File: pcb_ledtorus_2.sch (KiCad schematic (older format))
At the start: 15 parts, among them P1 CONN_02X04, P2 CONN_6, P3 MICRO-SD, P6 CONN_12, U4 STM32F46X_LQFP176, U5 US4881_HALL

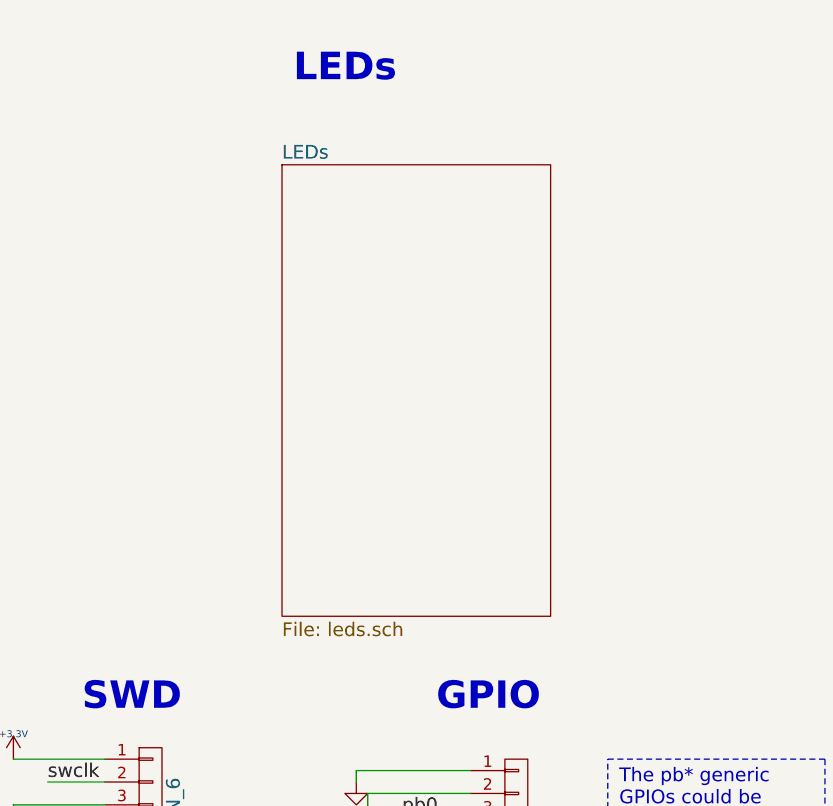
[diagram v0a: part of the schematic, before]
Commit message: Fix sin/sclk/sout/lat/gsclk 1-6 pins and labels.
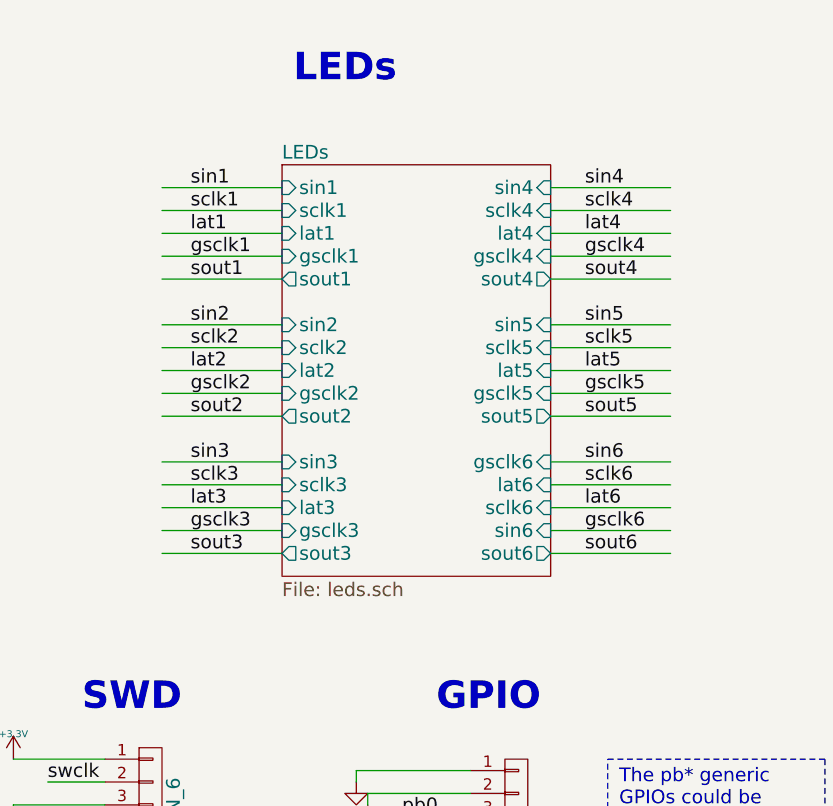
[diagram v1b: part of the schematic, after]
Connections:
- net labels added: lat4, lat5, lat6
- wire segments 128 -> 158
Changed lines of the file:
@@
 	5600 1600 5250 1600
 $Sheet
-S 8675 1675 1175 1975
+S 8675 1675 1175 1800
 U 5636686F
 F0 "LEDs" 60
 F1 "leds.sch" 60
+F2 "gsclk1" I L 8675 2075 60
+F3 "lat1" I L 8675 1975 60
+F4 "sclk1" I L 8675 1875 60
+F5 "sin1" I L 8675 1775 60
+F6 "sout1" O L 8675 2175 60
+F7 "gsclk2" I L 8675 2675 60
+F8 "lat2" I L 8675 2575 60
+F9 "sclk2" I L 8675 2475 60
+F10 "sin2" I L 8675 2375 60
+F11 "sout2" O L 8675 2775 60
+F12 "gsclk3" I L 8675 3275 60
+F13 "lat3" I L 8675 3175 60
+F14 "sclk3" I L 8675 3075 60
+F15 "sin3" I L 8675 2975 60
+F16 "sout3" O L 8675 3375 60
+F17 "gsclk4" I R 9850 2075 60
+F18 "lat4" I R 9850 1975 60
+F19 "sclk4" I R 9850 1875 60
+F20 "sin4" I R 9850 1775 60
+F21 "sout4" O R 9850 2175 60
+F22 "gsclk5" I R 9850 2675 60
+F23 "lat5" I R 9850 2575 60
+F24 "sclk5" I R 9850 2475 60
+F25 "sin5" I R 9850 2375 60
+F26 "sout5" O R 9850 2775 60
+F27 "gsclk6" I R 9850 2975 60
+F28 "lat6" I R 9850 3075 60
+F29 "sclk6" I R 9850 3175 60
+F30 "sin6" I R 9850 3275 60
+F31 "sout6" O R 9850 3375 60
 $EndSheet
+Wire Wire Line
+	8675 1775 8150 1775
+Wire Wire Line
+	8675 1875 8150 1875
+Wire Wire Line
+	8675 1975 8150 1975
+Wire Wire Line
+	8675 2075 8150 2075
+Wire Wire Line
+	8675 2175 8150 2175
+Wire Wire Line
+	8675 2375 8150 2375
+Wire Wire Line
+	8675 2475 8150 2475
+Wire Wire Line
+	8675 2575 8150 2575
+Wire Wire Line
+	8675 2675 8150 2675
+Wire Wire Line
+	8675 2775 8150 2775
+Wire Wire Line
+	8675 2975 8150 2975
+Wire Wire Line
+	8675 3075 8150 3075
+Wire Wire Line
+	8675 3175 8150 3175
+Wire Wire Line
+	8675 3275 8150 3275
+Wire Wire Line
+	8675 3375 8150 3375
+Wire Wire Line
+	10375 1775 9850 1775
+Wire Wire Line
+	10375 1875 9850 1875
+Wire Wire Line
+	10375 1975 9850 1975
+Wire Wire Line
+	10375 2075 9850 2075
+Wire Wire Line
+	10375 2175 9850 2175
+Wire Wire Line
+	10375 2375 9850 2375
+Wire Wire Line
+	10375 2475 9850 2475
+Wire Wire Line
+	10375 2575 9850 2575
+Wire Wire Line
+	10375 2675 9850 2675
+Wire Wire Line
+	10375 2775 9850 2775
+Wire Wire Line
+	10375 2975 9850 2975
+Wire Wire Line
+	10375 3075 9850 3075
+Wire Wire Line
+	10375 3175 9850 3175
+Wire Wire Line
+	10375 3275 9850 3275
+Wire Wire Line
+	10375 3375 9850 3375
+Text Label 8275 1775 0    60   ~ 0
+sin1
+Text Label 8275 2375 0    60   ~ 0
+sin2
+Text Label 8275 2975 0    60   ~ 0
+sin3
+Text Label 8275 1875 0    60   ~ 0
+sclk1
+Text Label 8275 2475 0    60   ~ 0
+sclk2
+Text Label 8275 3075 0    60   ~ 0
+sclk3
+Text Label 8275 1975 0    60   ~ 0
+lat1
+Text Label 8275 2575 0    60   ~ 0
+lat2
+Text Label 8275 3175 0    60   ~ 0
+lat3
+Text Label 8275 2075 0    60   ~ 0
+gsclk1
+Text Label 8275 2675 0    60   ~ 0
+gsclk2
+Text Label 8275 3275 0    60   ~ 0
+gsclk3
+Text Label 8275 2175 0    60   ~ 0
+sout1
+Text Label 8275 2775 0    60   ~ 0
+sout2
+Text Label 8275 3375 0    60   ~ 0
+sout3
+Text Label 10000 1775 0    60   ~ 0
+sin4
+Text Label 10000 2375 0    60   ~ 0
+sin5
+Text Label 10000 2975 0    60   ~ 0
+sin6
+Text Label 10000 1875 0    60   ~ 0
+sclk4
+Text Label 10000 2475 0    60   ~ 0
+sclk5
+Text Label 10000 3075 0    60   ~ 0
+sclk6
+Text Label 10000 1975 0    60   ~ 0
+lat4
+Text Label 10000 2575 0    60   ~ 0
+lat5
+Text Label 10000 3175 0    60   ~ 0
+lat6
+Text Label 10000 2075 0    60   ~ 0
+gsclk4
+Text Label 10000 2675 0    60   ~ 0
+gsclk5
+Text Label 10000 3275 0    60   ~ 0
+gsclk6
+Text Label 10000 2175 0    60   ~ 0
+sout4
+Text Label 10000 2775 0    60   ~ 0
+sout5
+Text Label 10000 3375 0    60   ~ 0
+sout6
 $EndSCHEMATC

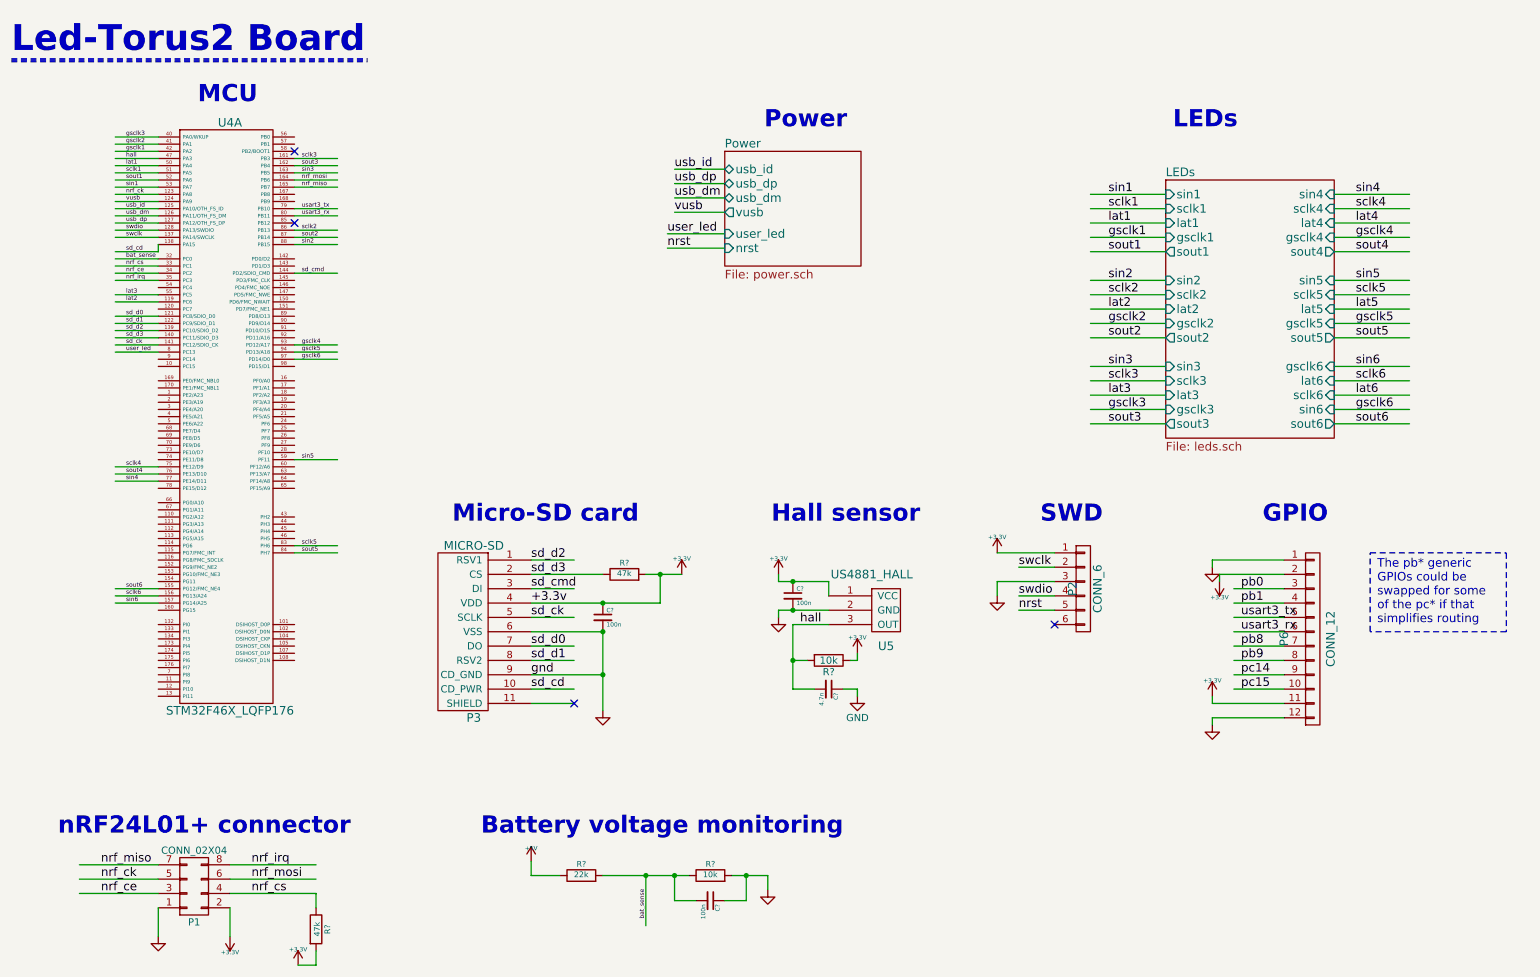
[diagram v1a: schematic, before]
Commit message: Fix alignment of everything to 50 mil
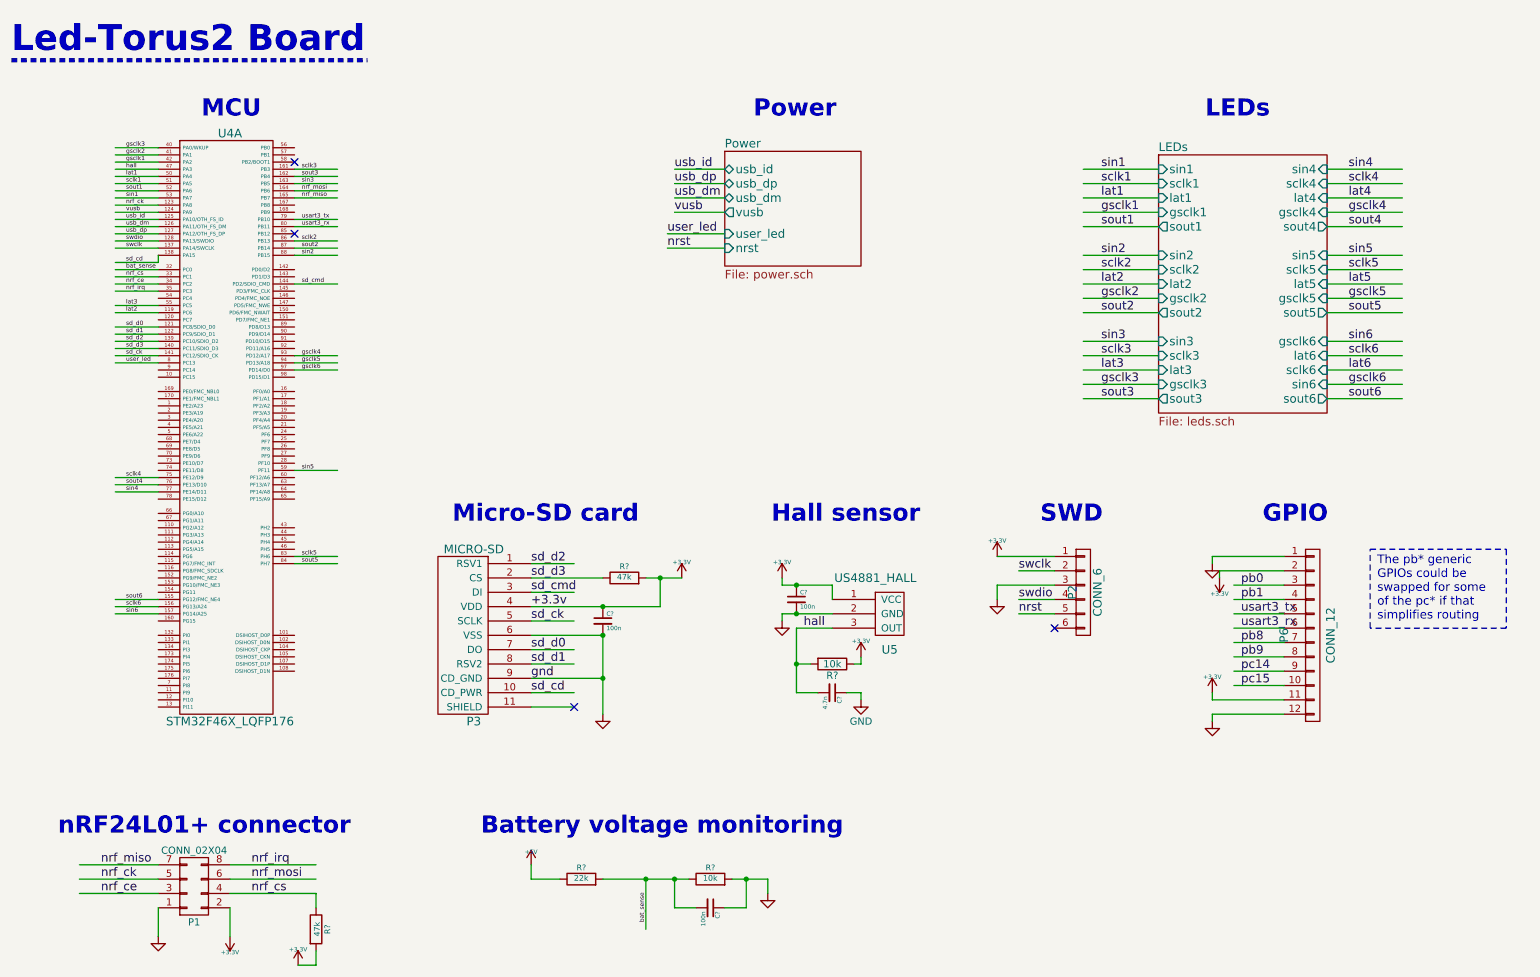
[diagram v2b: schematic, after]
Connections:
- wire segments 158 -> 167
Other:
- moved on the sheet: C?, P2, P3, P6, R?, U4A, U5

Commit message: Misc. small fixes, DRC (almost) passes now.
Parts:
- gave numbers to parts that had none: 9
- renumbered U4 to U1, U5 to U2
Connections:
- net labels removed: pb0, pb1, pb8, pb9, pc14, pc15
- wire segments 167 -> 155
- no-connect marks 4 -> 89

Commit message: Couple small fixes and tweaks.
Some resistors added on inputs connected directly to power lines.
Few labels added.
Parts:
- added R8: 10k, symbol R_Small
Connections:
- net labels added: usb_5v
- wire segments 155 -> 156
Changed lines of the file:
@@
 user_led
 Text Label 5250 1900 0    60   ~ 0
-vusb
+usb_5v
 Text Label 5200 2150 0    60   ~ 0
 nrst
@@
 Text Label 2650 4250 0    30   ~ 0
 lat6
+$Comp
+L R_Small R8
+U 1 1 5638A770
+P 1250 1900
+F 0 "R8" H 1280 1920 30  0000 L CNN
+F 1 "10k" V 1250 1850 30  0000 L CNN
+F 2 "" H 1250 1900 60  0000 C CNN
+F 3 "" H 1250 1900 60  0000 C CNN
+	1    1250 1900
+	0    1    1    0
+$EndComp
+Wire Wire Line
+	1150 1900 975  1900
+Text Label 1000 1900 0    30   ~ 0
+usb_5v
 $EndSCHEMATC

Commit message: Basic netlist with footprint assignment and import into pcbnew
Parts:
- P1: footprint (none) -> w_pin_strip:pin_socket_4x2
- R8: footprint (none) -> w_smd_resistors:r_0805
- U1: footprint (none) -> w_smd_lqfp:LQFP-176
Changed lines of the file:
@@
 F 0 "U1" H 2150 5450 60  0000 C CNN
 F 1 "STM32F46X_LQFP176" H 2150 1350 60  0000 C CNN
-F 2 "" H 2150 3700 60  0000 C CNN
+F 2 "w_smd_lqfp:LQFP-176" H 2150 3700 60  0001 C CNN
 F 3 "" H 2150 3700 60  0000 C CNN
 	1    2150 3400
@@
 F 0 "P1" H 1900 6850 50  0000 C CNN
 F 1 "CONN_02X04" H 1900 6350 50  0000 C CNN
-F 2 "" H 1900 5400 60  0000 C CNN
+F 2 "w_pin_strip:pin_socket_4x2" H 1900 5400 60  0001 C CNN
 F 3 "" H 1900 5400 60  0000 C CNN
 	1    1900 6600
@@
 F 0 "R8" H 1280 1920 30  0000 L CNN
 F 1 "10k" V 1250 1850 30  0000 L CNN
-F 2 "" H 1250 1900 60  0000 C CNN
+F 2 "w_smd_resistors:r_0805" H 1250 1900 60  0001 C CNN
 F 3 "" H 1250 1900 60  0000 C CNN
 	1    1250 1900

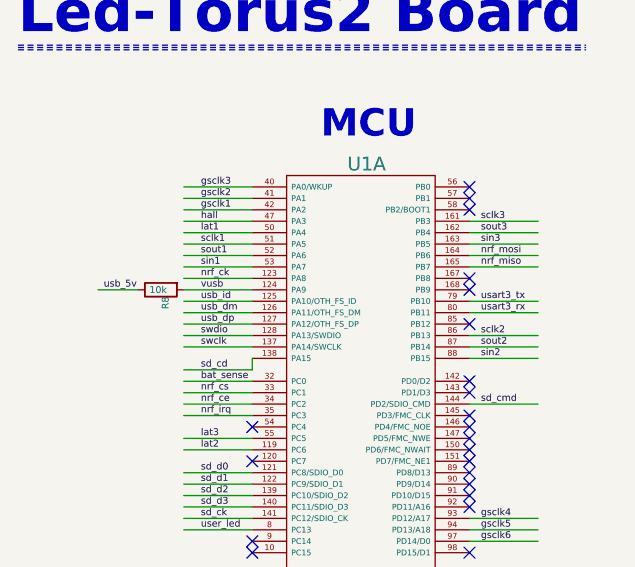
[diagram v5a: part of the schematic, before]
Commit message: Small component changes.
Fix couple of missing footprints. Make 100nF caps 0603.

Some very rough component placement to avoid overlap.
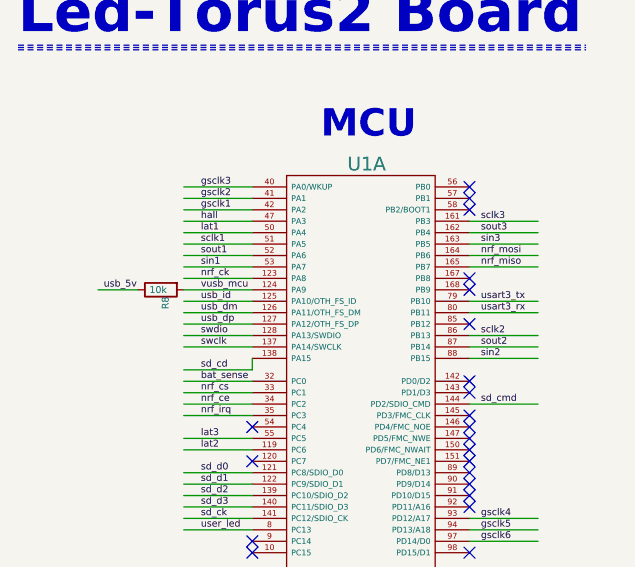
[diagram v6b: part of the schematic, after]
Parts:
- C1, C2, C4: footprint w_smd_cap:c_0805 -> w_smd_cap:c_0603
- U2: footprint Discret:TO92 -> TO_SOT_Packages_THT:TO-92_Inline_Narrow_Oval
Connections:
- net labels added: vusb_mcu
- net labels removed: vusb
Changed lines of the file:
@@
 F 0 "C2" H 4775 4800 30  0000 L CNN
 F 1 "100n" H 4775 4700 30  0000 L CNN
-F 2 "w_smd_cap:c_0805" H 4750 4750 60  0001 C CNN
+F 2 "w_smd_cap:c_0603" H 4750 4750 60  0001 C CNN
 F 3 "" H 4750 4750 60  0000 C CNN
 	1    4750 4750
@@
 F 0 "U2" H 6750 4350 60  0000 C CNN
 F 1 "US4881_HALL" H 6650 4850 60  0000 C CNN
-F 2 "Discret:TO92" H 6650 4650 60  0001 C CNN
+F 2 "TO_SOT_Packages_THT:TO-92_Inline_Narrow_Oval" H 6650 4650 60  0001 C CNN
 F 3 "" H 6650 4650 60  0000 C CNN
 	1    6650 4650
@@
 F 0 "C1" H 6125 4650 30  0000 L CNN
 F 1 "100n" H 6125 4550 30  0000 L CNN
-F 2 "w_smd_cap:c_0805" H 6100 4600 60  0001 C CNN
+F 2 "w_smd_cap:c_0603" H 6100 4600 60  0001 C CNN
 F 3 "" H 6100 4600 60  0000 C CNN
 	1    6100 4600
@@
 F 0 "C4" H 5525 6800 30  0000 L CNN
 F 1 "100n" H 5525 6700 30  0000 L CNN
-F 2 "w_smd_cap:c_0805" H 5500 6750 60  0001 C CNN
+F 2 "w_smd_cap:c_0603" H 5500 6750 60  0001 C CNN
 F 3 "" H 5500 6750 60  0000 C CNN
 	1    5500 6750
@@
 usb_dp
 Text Label 1425 1900 0    30   ~ 0
-vusb
+vusb_mcu
 Text Label 1425 2700 0    30   ~ 0
 sd_d0
